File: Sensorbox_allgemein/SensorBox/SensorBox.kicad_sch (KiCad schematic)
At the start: 26 parts, among them J1 SD_Card, SW1 SW_SPST, U1 BME280, U2 PS1-O3-100, U3 Beetle ESP32-C6, U4 MC33063AD, U6 MAX31855EASA, U8 HPP845E131R5

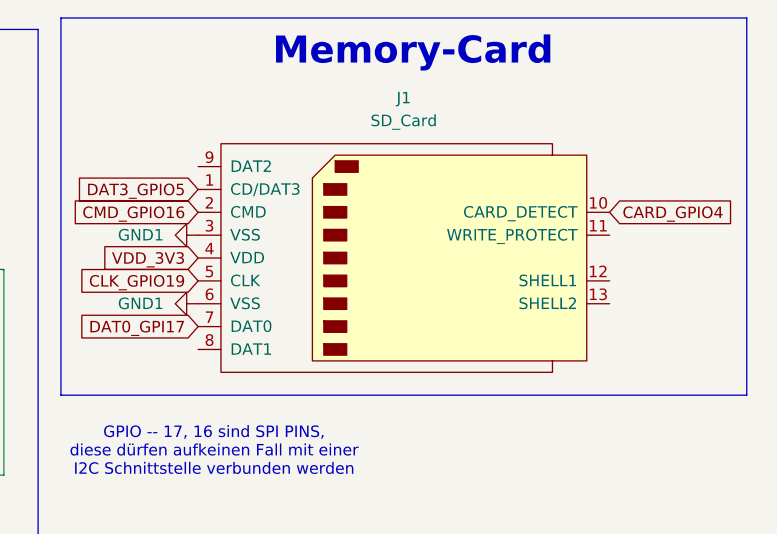
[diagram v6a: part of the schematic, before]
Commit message: Lib
library erschaffen bezüglich dem sd modul zum ablesen und schreiben

plus im hauptschaltplan eingesetzt
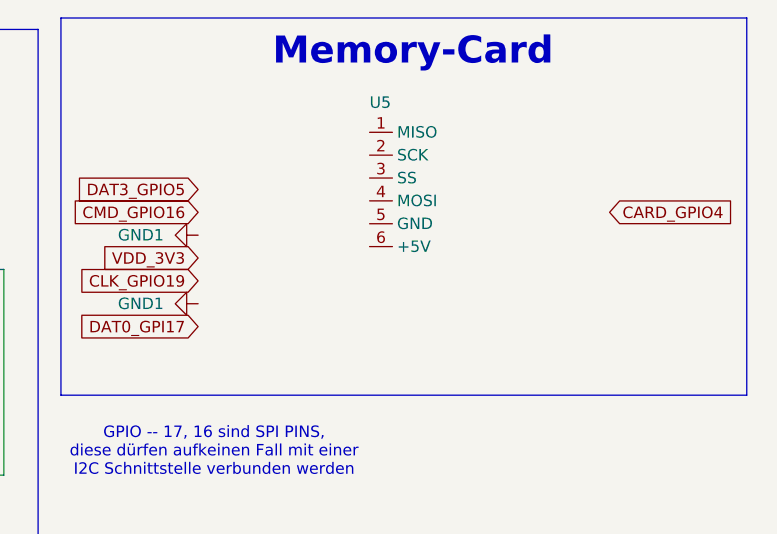
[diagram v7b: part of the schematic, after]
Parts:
- removed J1: SD_Card, symbol Connector:SD_Card
- added U5: ~, Connector_PinHeader_2.54mm:PinHeader_1x06_P2.54mm_Vertical, symbol SD_Card_Module:Modul_Fermion
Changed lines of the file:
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@@
+	)
+	(symbol
+		(lib_id "SD_Card_Module:Modul_Fermion")
+		(at 240.03 26.67 0)
+		(unit 1)
+		(exclude_from_sim no)
+		(in_bom yes)
+		(on_board yes)
+		(dnp no)
+		(property "Reference" "U5"
+			(at 240.03 23.368 0)
+			(effects
+				(font
+					(size 1.27 1.27)
+				)
+				(justify left)
+			)
+		)
+		(property "Value" "~"
+			(at 243.84 34.29 0)
+			(effects
+				(font
+					(size 1.27 1.27)
+				)
+				(justify left)
+			)
+		)
+		(property "Footprint" "Connector_PinHeader_2.54mm:PinHeader_1x06_P2.54mm_Vertical"
+			(at 240.03 26.67 0)
+			(effects
+				(font
+					(size 1.27 1.27)
+				)
+				(hide yes)
+			)
+		)
+		(property "Datasheet" ""
+			(at 240.03 26.67 0)
+			(effects
+				(font
+					(size 1.27 1.27)
+				)
+				(hide yes)
+			)
+		)
+		(property "Description" ""
+			(at 240.03 26.67 0)
+			(effects
+				(font
+					(size 1.27 1.27)
+				)
+				(hide yes)
+			)
+		)
+		(pin "4"
+		)
+		(pin "6"
+		)
+		(pin "1"
+		)
+		(pin "2"
+		)
+		(pin "3"
+		)
+		(pin "5"
+		)
+		(instances
+			(project "SensorBox"
+				(path "/7cbe8151-7294-42e6-9c4e-6ec8952d674f"
+					(reference "U5")
+					(unit 1)
+				)
+			)
+		)
 	)
 	(symbol
@@
 					(unit 1)
 				)
-			)
-		)
-	)
-	(symbol
-		(lib_id "Connector:SD_Card")
-		(at 243.84 40.64 0)
-		(unit 1)
-		(exclude_from_sim no)
-		(in_bom yes)
-		(on_board yes)
-		(dnp no)
-		(fields_autoplaced yes)
-		(property "Reference" "J1"
-			(at 243.84 22.86 0)
-			(effects
-				(font
-					(size 1.27 1.27)
-				)
-			)
-		)
-		(property "Value" "SD_Card"
-			(at 243.84 25.4 0)
-			(effects
-				(font
-					(size 1.27 1.27)
-				)
-			)
-		)
-		(property "Footprint" ""
-			(at 243.84 40.64 0)
-			(effects
-				(font
-					(size 1.27 1.27)
-				)
-				(hide yes)
-			)
-		)
-		(property "Datasheet" "http://portal.fciconnect.com/Comergent//fci/drawing/10067847.pdf"
-			(at 243.84 40.64 0)
-			(effects
-				(font
-					(size 1.27 1.27)
-				)
-				(hide yes)
-			)
-		)
-		(property "Description" "SD Card Reader"
-			(at 243.84 40.64 0)
-			(effects
-				(font
-					(size 1.27 1.27)
-				)
-				(hide yes)
-			)
-		)
-		(pin "10"
-		)
-		(pin "13"
-		)
-		(pin "4"
-		)
-		(pin "11"
-		)
-		(pin "12"
-		)
-		(pin "3"
-		)
-		(pin "5"
-		)
-		(pin "6"
-		)
-		(pin "7"
-		)
-		(pin "1"
-		)
-		(pin "2"
-		)
-		(pin "8"
-		)
-		(pin "9"
-		)
-		(instances
-			(project "SensorBox"
-				(path "/7cbe8151-7294-42e6-9c4e-6ec8952d674f"
-					(reference "J1")
-					(unit 1)
-				)

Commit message: Test
.
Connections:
- net CARD_GPIO4: no longer names the net of U3.3 (GPIO4)
- net CMD_GPIO16: no longer names the net of U3.12 (GPIO16)
- net DAT0_GPIO17: no longer names the net of U3.13 (GPIO17)
- net DAT3_GPIO5: no longer names the net of U3.4 (GPIO5)
